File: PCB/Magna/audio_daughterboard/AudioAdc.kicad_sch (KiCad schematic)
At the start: 24 parts, among them J301 PSG01550, U301 WM8782SEDS

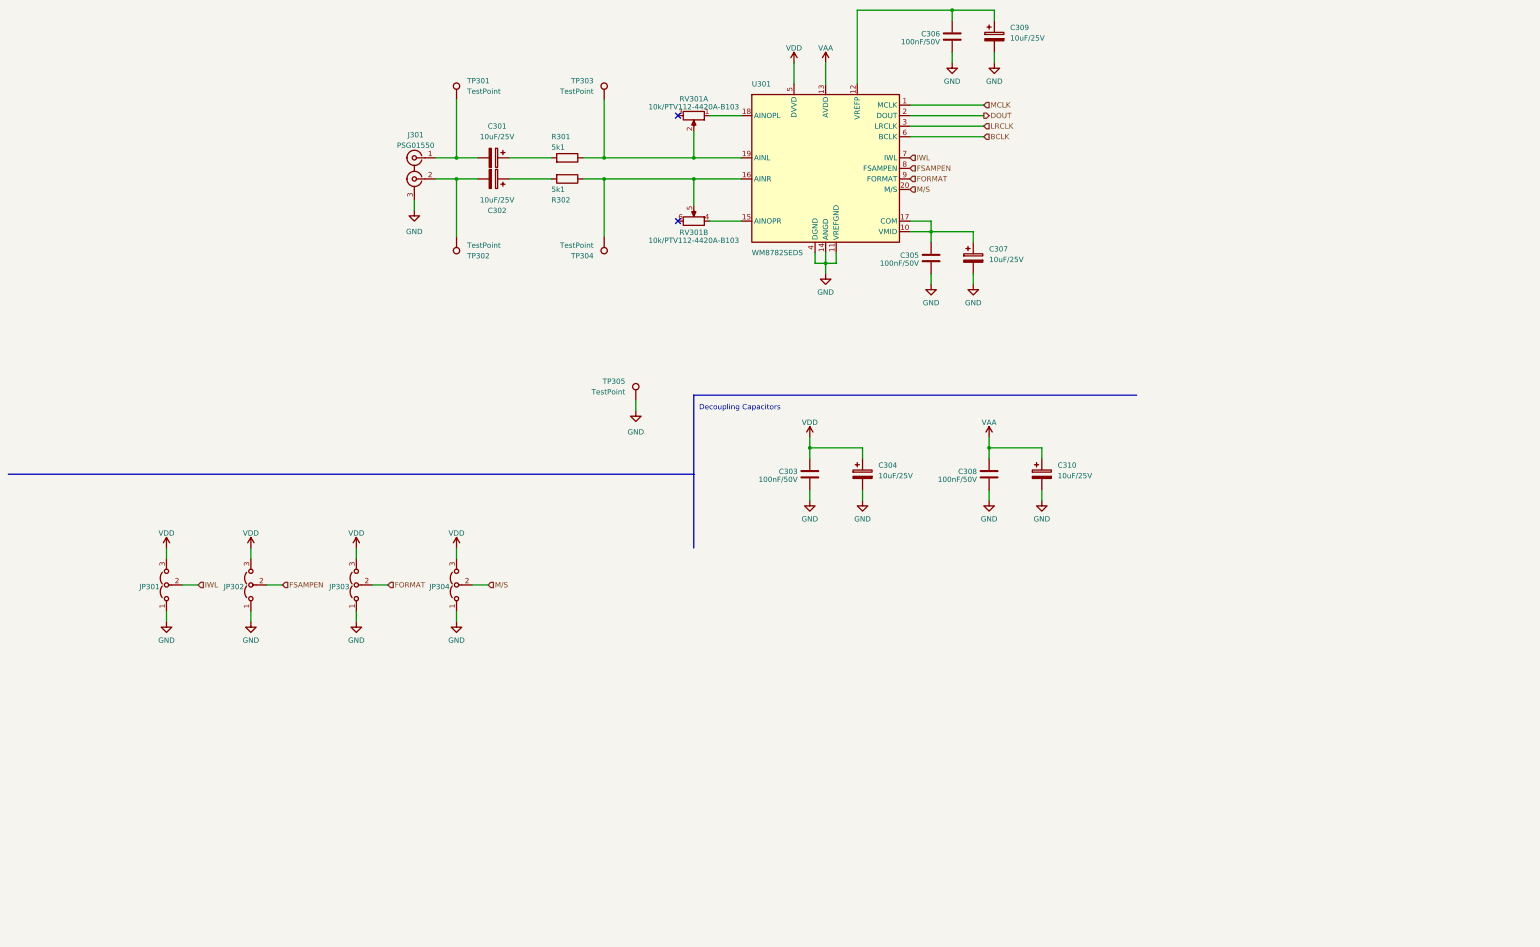
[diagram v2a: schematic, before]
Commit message: Start of redesign of Audio board
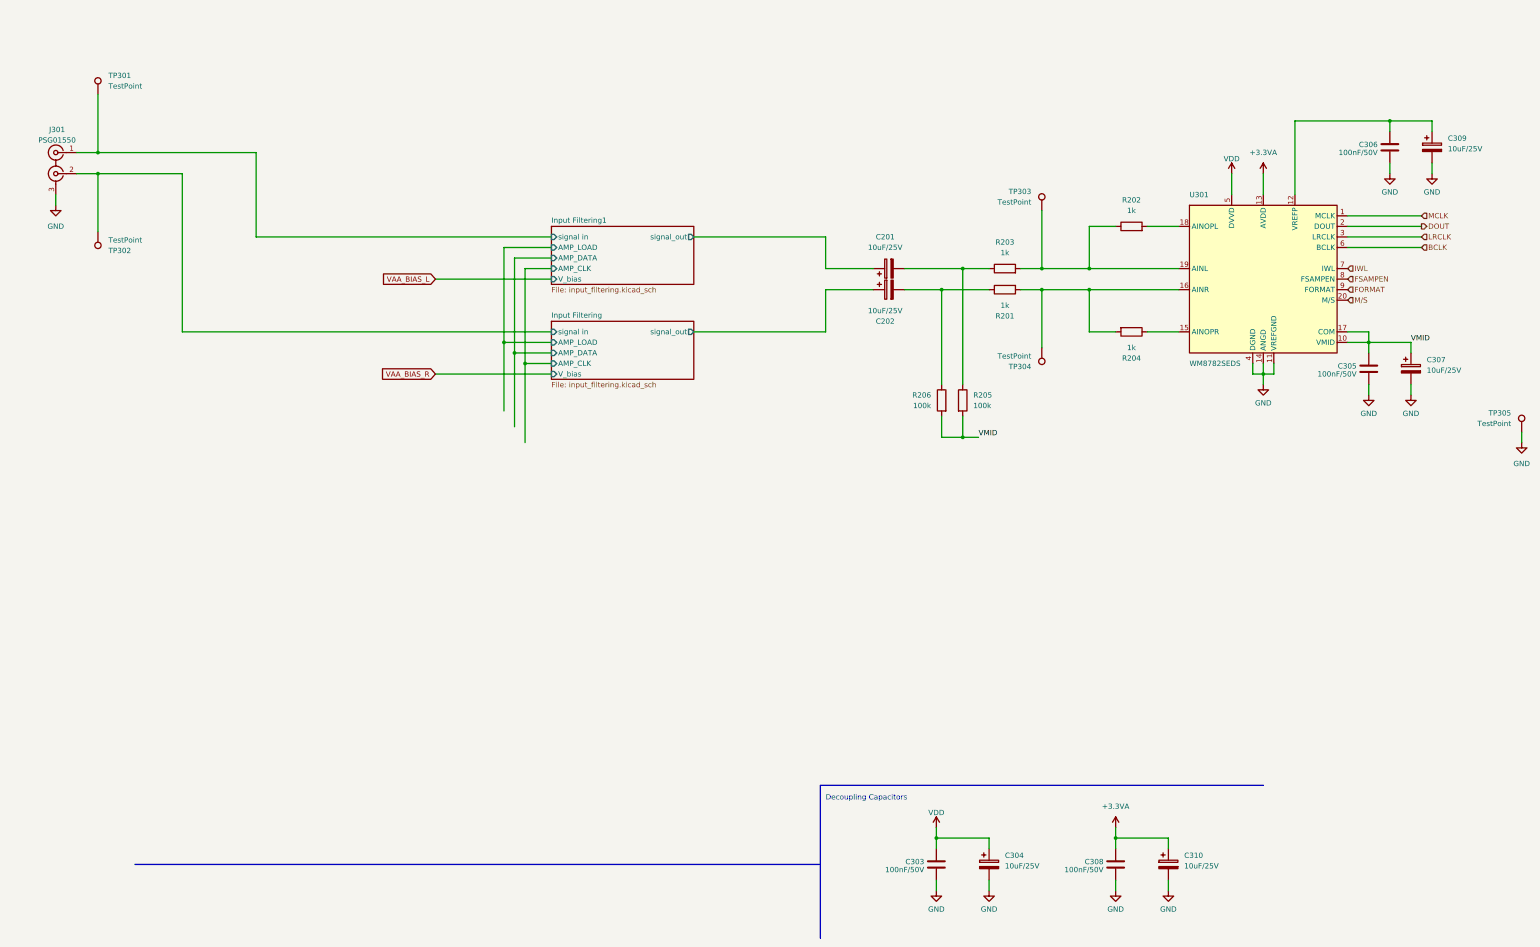
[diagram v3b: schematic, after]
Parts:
- removed C301, C302: 10uF/25V, Capacitor_SMD:CP_Elec_4x5.8, symbol Device:C_Polarized
- removed JP301, JP302, JP303, JP304: SolderJumper_3_Bridged12, Jumper:SolderJumper-3_P2.0mm_Open_TrianglePad1.0x1.5mm_NumberLabels, symbol Jumper:Jumper_3_Open
- removed R301, R302: 5k1, Resistor_SMD:R_0805_2012Metric_Pad1.20x1.40mm_HandSolder, symbol Device:R
- removed RV301: 10k/PTV112-4420A-B103, Skrooter_footprints:Potentiometer_Bourns_PTV09A-1_Dual_Vertical, symbol Device:R_Potentiometer_Dual_Separate
- added C201, C202: 10uF/25V, Capacitor_SMD:CP_Elec_4x5.8, symbol Device:C_Polarized
- added R201, R202, R203, R204: 1k, symbol Device:R
- added R205, R206: 100k, symbol Device:R
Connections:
- net at TP304.1, U301.16 (AINR): now also R201.2, R204.2
- net Input Filtering/signal in: now reaches J301.2 (IN2), TP302.1
- net at TP303.1, U301.19 (AINL): now also R202.1, R203.2
- net Input Filtering1/signal in: now reaches J301.1 (IN1), TP301.1
- net VMID: now reaches C305.1, C307.1, U301.10 (VMID), U301.17 (COM)
- net VMID: now also R205.2, R206.2
- net at U301.15 (AINOPR): now also R204.1
- net at U301.18 (AINOPL): now also R202.2
- net VAA renamed +3.3VA
- new net: C201.2, R203.1, R205.1
- new net: C202.2, R201.1, R206.1
- new net Input Filtering/signal_out: C202.1
- new net Input Filtering1/signal_out: C201.1
- no-connect marks 2 -> 0
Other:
- added sheet Input Filtering (input_filtering.kicad_sch)
- added sheet Input Filtering1 (input_filtering.kicad_sch)
- moved on the sheet: C303, C304, C305, C306, C307, C308, C309, C310, J301, TP301, TP302, TP303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

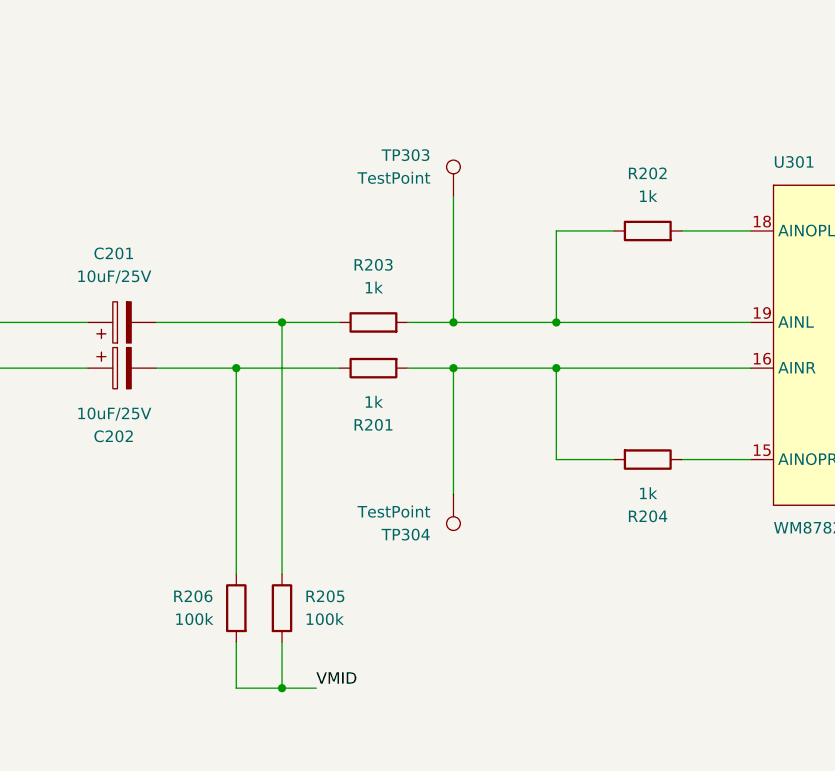
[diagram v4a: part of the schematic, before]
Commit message: Finish simulations and design of input filtering
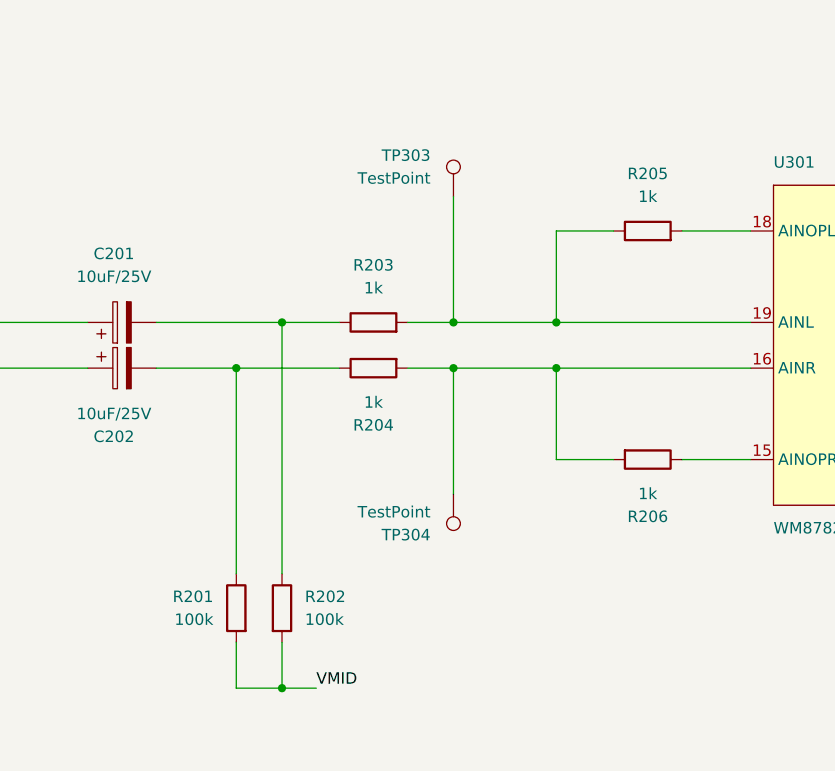
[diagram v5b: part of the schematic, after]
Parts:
- renumbered R206 to R201, R205 to R202, R201 to R204, R202 to R205, R204 to R206

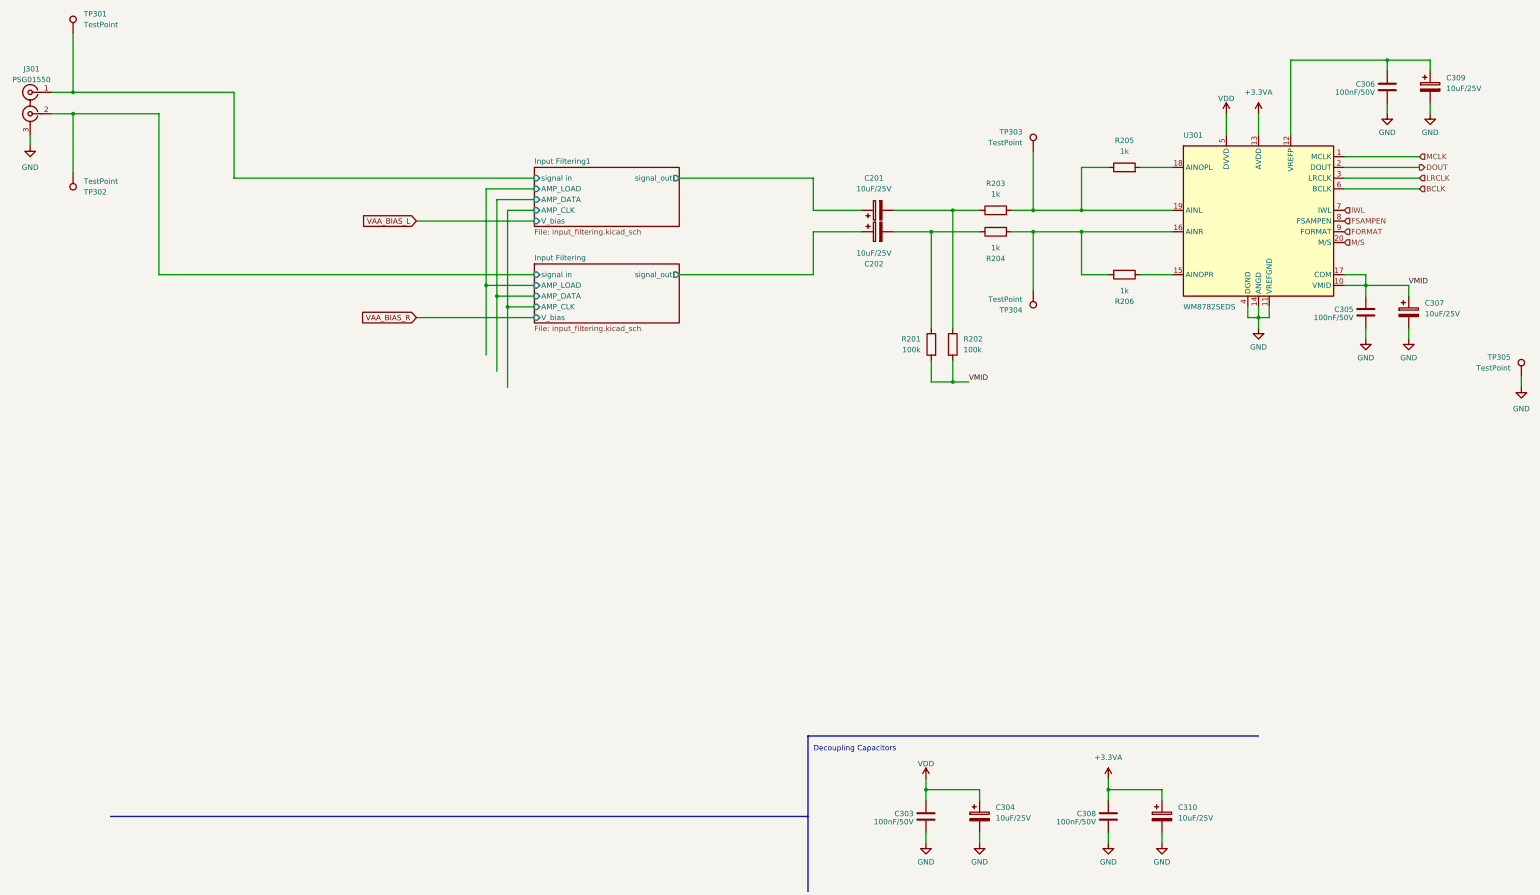
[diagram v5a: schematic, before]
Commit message: Change ADC and add MCU for IO control
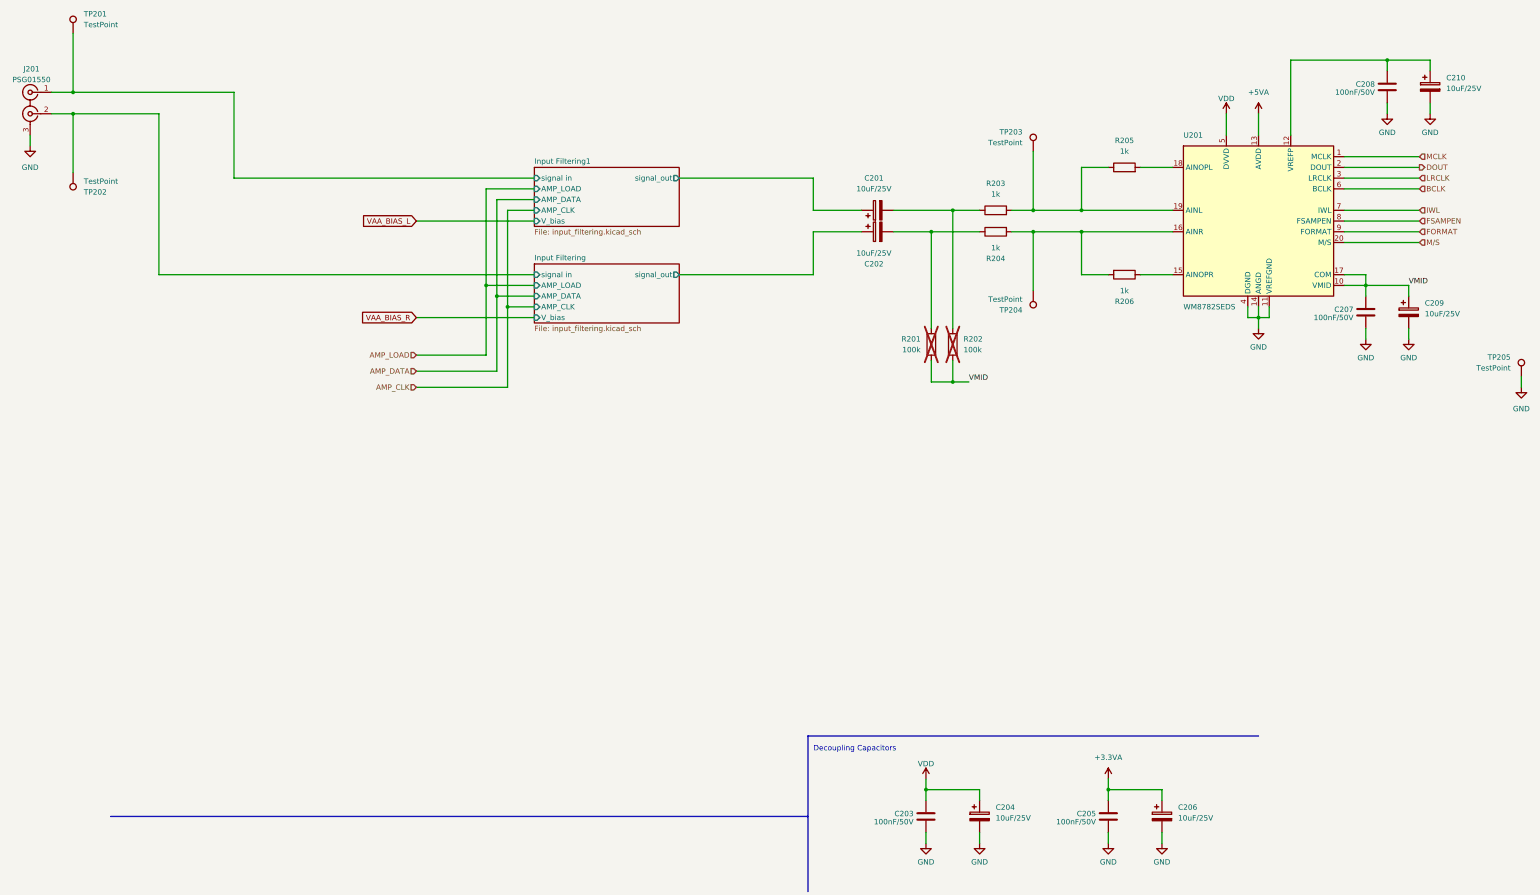
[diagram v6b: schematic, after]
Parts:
- R201, R202: now not fitted; now left out of the parts list
- renumbered C303 to C203, C304 to C204, C308 to C205, C310 to C206, C305 to C207, C306 to C208, C307 to C209, C309 to C210, J301 to J201, TP301 to TP201, TP302 to TP202, TP303 to TP203, TP304 to TP204, TP305 to TP205, U301 to U201
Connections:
- net +3.3VA: no longer U201.13 (AVDD)
- new net +5VA: U201.13 (AVDD)

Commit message: Update schematics to Kicad 9
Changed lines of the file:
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@@
 					(size 1.27 1.27)
 				)
+				(hide yes)
 			)
 		)
@@
 					(size 1.27 1.27)
 				)
+				(hide yes)
 			)
 		)
@@
 					(size 1.27 1.27)
 				)
+				(hide yes)
 			)
 		)
@@
 					(size 1.27 1.27)
 				)
+				(hide yes)
 			)
 		)
@@
 					(size 1.27 1.27)
 				)
+				(hide yes)
 			)
 		)
@@
 					(size 1.27 1.27)
 				)
+				(hide yes)
 			)
 		)
@@
 					(size 1.27 1.27)
 				)
+				(hide yes)
 			)
 		)
@@
 					(size 1.27 1.27)
 				)
+				(hide yes)
 			)
 		)
@@
 					(size 1.27 1.27)
 				)
+				(hide yes)
 			)
 		)
@@
 					(size 1.27 1.27)
 				)
+				(hide yes)
 			)
 		)
@@
 					(size 1.27 1.27)
 				)
+				(hide yes)
 			)
 		)
@@
 					(size 1.27 1.27)
 				)
+				(hide yes)
 			)
 		)
@@
 					(size 1.27 1.27)
 				)
+				(hide yes)
 			)
 		)
@@
 					(size 1.27 1.27)
 				)
+				(hide yes)
 			)
 		)
@@
 					(size 1.27 1.27)
 				)
+				(hide yes)
 			)
 		)
@@
 					(size 1.27 1.27)
 				)
+				(hide yes)
 			)
 		)
@@
 					(size 1.27 1.27)
 				)
+				(hide yes)
 			)
 		)
@@
 					(size 1.27 1.27)
 				)
+				(hide yes)
 			)
 		)
@@
 					(size 1.27 1.27)
 				)
+				(hide yes)
 			)
 		)
@@
 					(size 1.27 1.27)
 				)
+				(hide yes)
 			)
 		)
@@
 					(size 1.27 1.27)
 				)
+				(hide yes)
 			)
 		)
@@
 					(size 1.27 1.27)
 				)
+				(hide yes)
 			)
 		)
@@
 					(size 1.27 1.27)
 				)
+				(hide yes)
 			)
 		)
@@
 					(size 1.27 1.27)
 				)
+				(hide yes)
 			)
 		)
@@
 					(size 1.27 1.27)
 				)
+				(hide yes)
 			)
 		)
@@
 					(size 1.27 1.27)
 				)
+				(hide yes)
 			)
 		)
@@
 					(size 1.27 1.27)
 				)
+				(hide yes)
 			)
 		)
@@
 					(size 1.27 1.27)
 				)
+				(hide yes)
 			)
 		)
@@
 					(size 1.27 1.27)
 				)
+				(hide yes)
 			)
 		)
@@
 					(size 1.27 1.27)
 				)
+				(hide yes)
 			)
 		)
@@
 					(size 1.27 1.27)
 				)
+				(hide yes)
 			)
 		)
@@
 					(size 1.27 1.27)
 				)
+				(hide yes)
 			)
 		)
@@
 					(size 1.27 1.27)
 				)
-			)
-		)
+				(hide yes)
+			)
+		)
